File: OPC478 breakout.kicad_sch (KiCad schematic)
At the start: 16 parts, among them J1 Conn_01x05_Pin, J2 AudioPlug4, J3 Conn_01x01_Socket, J4 Conn_01x01_Socket, Q1 BC557, Q2 BC547

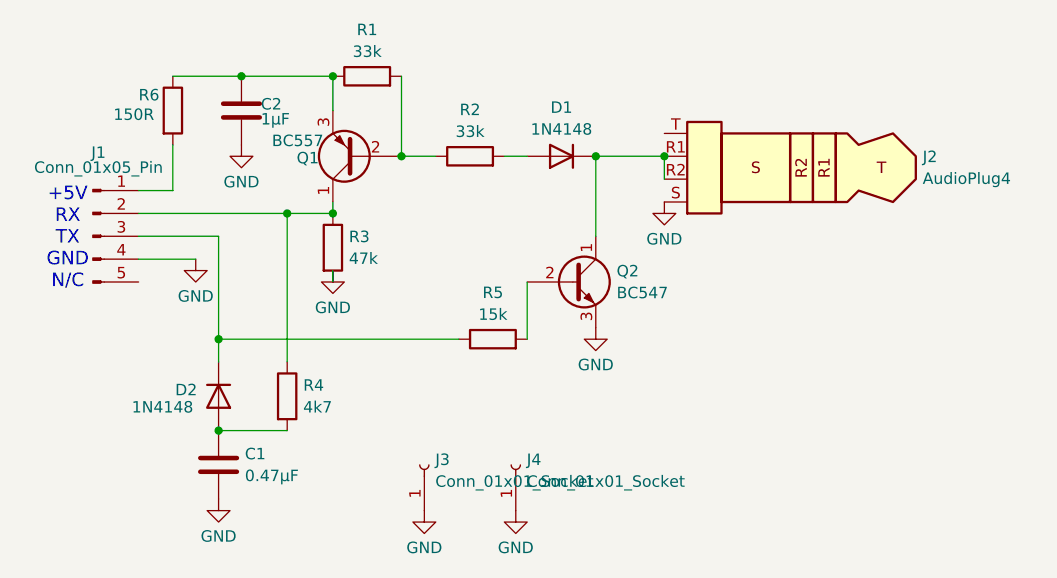
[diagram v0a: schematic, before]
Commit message: remove no-longer needed jumper from schematic
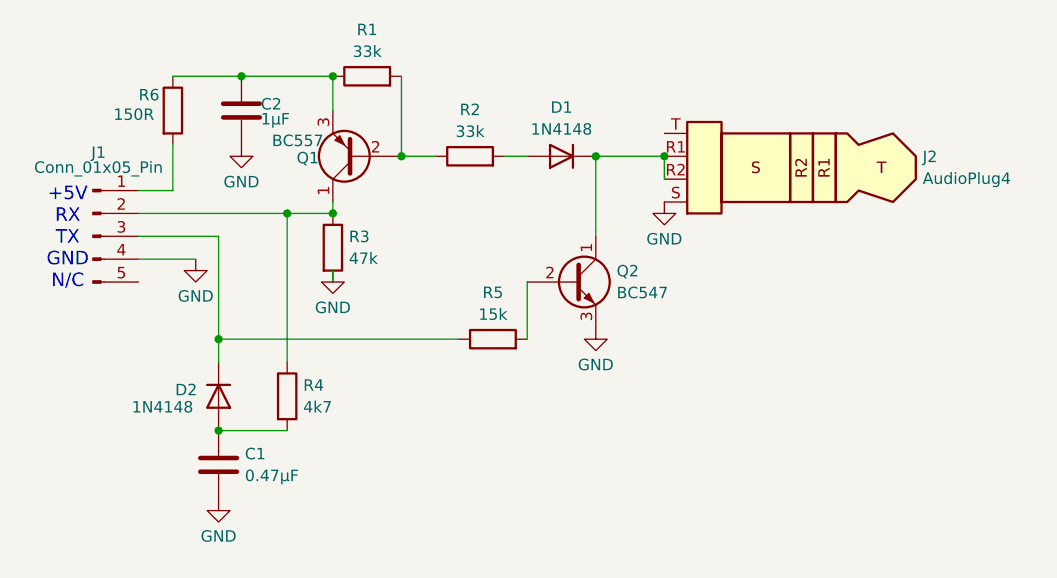
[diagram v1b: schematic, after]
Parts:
- removed J3, J4: Conn_01x01_Socket, Connector_PinHeader_2.54mm:PinHeader_1x01_P2.54mm_Vertical, symbol Connector:Conn_01x01_Socket
